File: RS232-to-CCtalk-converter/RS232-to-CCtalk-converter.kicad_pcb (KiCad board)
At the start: 2 copper layers, 23 parts, among them J1 DB9_Male, J2 Conn_01x04, J3 Conn_01x03, Q1 BC847, Q2 BC856A-QR, U1 ST232BDR, U2 UA78M05

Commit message: inital adding
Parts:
- C1, C2, C3, C4, C5, C6, C7, C8, C9: footprint Capacitor_SMD:C_0201_0603Metric -> RS232-to-CCtalk-converter-lib:C_0603_1608Metric
- D1, D2: footprint Diode_SMD:D_SOD-323F -> RS232-to-CCtalk-converter-lib:D_SOD-323F
- J1: footprint Connector_Dsub:DSUB-9_Male_EdgeMount_P2.77mm -> RS232-to-CCtalk-converter-lib:DSUB-9_Male_EdgeMount_P2.77mm
- J2: footprint Connector:FanPinHeader_1x04_P2.54mm_Vertical -> RS232-to-CCtalk-converter-lib:FanPinHeader_1x04_P2.54mm_Vertical
- J3: footprint Connector:FanPinHeader_1x03_P2.54mm_Vertical -> RS232-to-CCtalk-converter-lib:FanPinHeader_1x03_P2.54mm_Vertical
- Q1: footprint Package_TO_SOT_SMD:SOT-23 -> RS232-to-CCtalk-converter-lib:SOT-23
- Q2: value BC856A-QR -> BC856; footprint Package_TO_SOT_SMD:SOT-23 -> RS232-to-CCtalk-converter-lib:SOT-23
- R1, R3, R4: value 10k -> 10K; footprint Resistor_SMD:R_0603_1608Metric -> RS232-to-CCtalk-converter-lib:R_0603_1608Metric
- R2: footprint Resistor_SMD:R_0603_1608Metric -> RS232-to-CCtalk-converter-lib:R_0603_1608Metric
- R5: value 100k -> 100K; footprint Resistor_SMD:R_0603_1608Metric -> RS232-to-CCtalk-converter-lib:R_0603_1608Metric
- U1: value ST232BDR -> ST232B; footprint Package_SO:SOIC-16_4.55x10.3mm_P1.27mm -> RS232-to-CCtalk-converter-lib:SOIC-16_4.55x10.3mm_P1.27mm
- U2: value UA78M05 -> L7805; footprint Package_TO_SOT_SMD:TO-252-3_TabPin2 -> RS232-to-CCtalk-converter-lib:TO-252-3_TabPin2
- moved D1 88.3 mm to (115.5, 100.4)
- moved U2 73.7 mm to (119.4, 94.9)
- moved Q1 46.8 mm to (160.9, 73.5)
- moved C7 44.0 mm to (160.5, 77.0)
- moved C5 41.5 mm to (165.3, 72.6)
- moved J3 30.4 mm to (147.1, 70.4)
- moved J2 28.4 mm to (144.8, 76.2)
- moved R1 28.2 mm to (158.0, 80.6)
- moved R2 24.4 mm to (145.2, 94.6)
- moved C4 16.4 mm to (148.3, 88.5)
- moved R4 14.4 mm to (152.3, 88.5)
- moved R3 14.2 mm to (165.3, 75.1)
- moved R5 9.15 mm to (146.1, 92.1)
- moved C6 7.78 mm to (141.2, 99.1)
- moved C1 7.62 mm to (137.2, 99.1)
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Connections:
- C1 pad 1: Net-(C1-Pad1) -> +5V
- C1 pad 2: +5V -> Net-(C1-Pad2)
- C2 pad 1: GNDREF -> Net-(C2-Pad1)
- C2 pad 2: Net-(C2-Pad2) -> GNDREF
- C3 pad 1: Net-(C3-Pad1) -> Net-(U1-Pad4)
- R1 pad 1: CCTALK-DATA -> +5V
- R1 pad 2: +5V -> CCTALK-DATA
- R4 pad 1: Net-(Q1-Pad1) -> Net-(Q2-Pad3)
- R4 pad 2: Net-(Q2-Pad3) -> Net-(Q1-Pad1)
- R5 pad 1: Net-(Q1-Pad1) -> GNDREF
- R5 pad 2: GNDREF -> Net-(Q1-Pad1)
- U1 pad 1: Net-(C6-Pad2) -> Net-(C6-Pad1)
- U1 pad 2: Net-(C1-Pad1) -> Net-(C1-Pad2)
- U1 pad 3: Net-(C6-Pad1) -> Net-(C6-Pad2)
- U1 pad 4: Net-(C3-Pad2) -> Net-(U1-Pad4)
- U1 pad 5: Net-(C3-Pad1) -> Net-(C3-Pad2)
- U1 pad 6: Net-(C2-Pad2) -> Net-(C2-Pad1)

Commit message: first milestone
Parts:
- C7, C8, C9, D2, U2: moved to B.Cu
- J3: value Conn_01x03 -> CCtalk Cable
- moved C5 62.3 mm to (109.5, 100.2), turned to 180 degrees
- moved R3 55.9 mm to (115.3, 100.0)
- moved Q1 42.9 mm to (123.2, 94.1)
- moved C4 41.0 mm to (109.5, 101.7), turned to 180 degrees
- moved C7 40.8 mm to (122.9, 93.1), turned to -90 degrees
- moved R1 34.7 mm to (126.6, 95.4)
- moved R4 32.5 mm to (120.5, 95.2), turned to 90 degrees
- moved J3 31.1 mm to (129.7, 96.2), turned to 90 degrees
- moved J2 29.2 mm to (117.7, 87.1), turned to 180 degrees
- moved R5 26.0 mm to (120.1, 92.2), turned to -90 degrees
- moved C1 25.1 mm to (112.1, 101.0), turned to 90 degrees
- moved C9 23.7 mm to (119.2, 98.1), turned to 180 degrees
- moved C6 22.8 mm to (118.5, 96.8), turned to 90 degrees
- moved C8 22.5 mm to (118.8, 99.6), turned to 180 degrees
- moved Q2 20.3 mm to (118.6, 100.1), turned to 65 degrees
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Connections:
- J3 pad 1: Net-(D2-Pad2) -> GNDREF
- J3 pad 3: GNDREF -> Net-(D2-Pad2)
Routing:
- net GNDREF: track 0.00 -> 77.8 mm, vias 0 -> 8
- net +5V: track 0.00 -> 29.3 mm, vias 0 -> 1
- net TX: track 0.00 -> 21.5 mm
- net RX: track 0.00 -> 17.4 mm, vias 0 -> 1
- net Net-(C1-Pad2): track 0.00 -> 8.53 mm
- net TXout: track 0.00 -> 8.46 mm, vias 0 -> 2
- net CCTALK-DATA: track 0.00 -> 5.36 mm
- net +24V: track 0.00 -> 4.56 mm
- net RXout: track 0.00 -> 4.55 mm
- net Net-(Q1-Pad1): track 0.00 -> 3.77 mm
- net Net-(Q2-Pad3): track 0.00 -> 3.62 mm
- net Net-(D2-Pad2): track 0.00 -> 3.14 mm
- net Net-(C6-Pad1): track 0.00 -> 2.18 mm
- net Net-(C2-Pad1): track 0.00 -> 2.00 mm
- net Net-(C3-Pad2): track 0.00 -> 1.93 mm
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- added copper zone on B.Cu, net GNDREF
- added copper zone on F.Cu, net GNDREF
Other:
- board outline added: 30.4 x 16.9 mm
- board text added: "+24 CC GND"

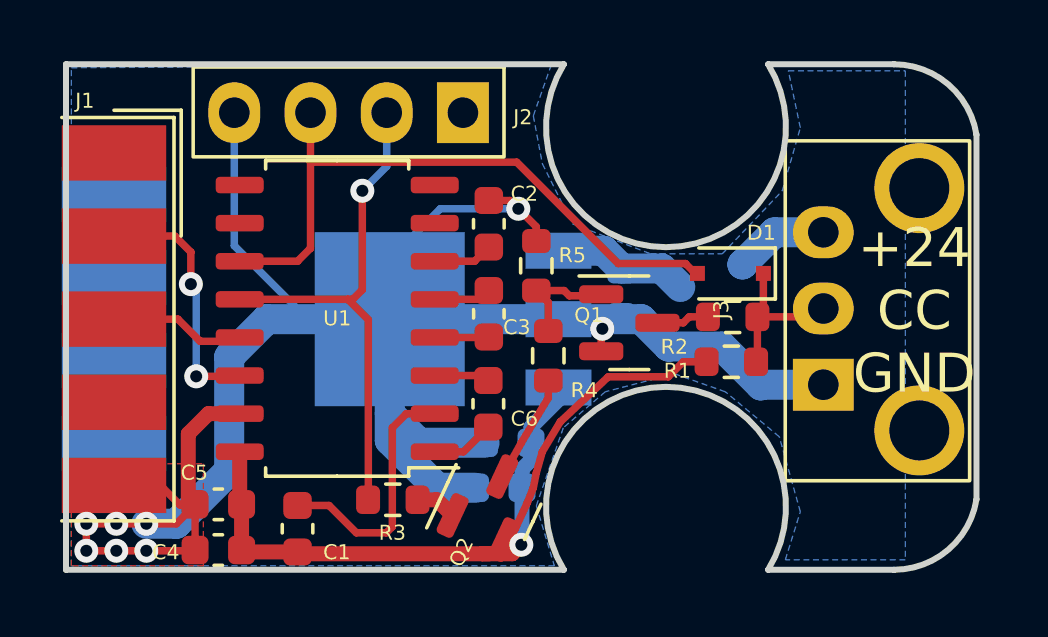
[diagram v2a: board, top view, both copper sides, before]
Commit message: add +5v to debug connector
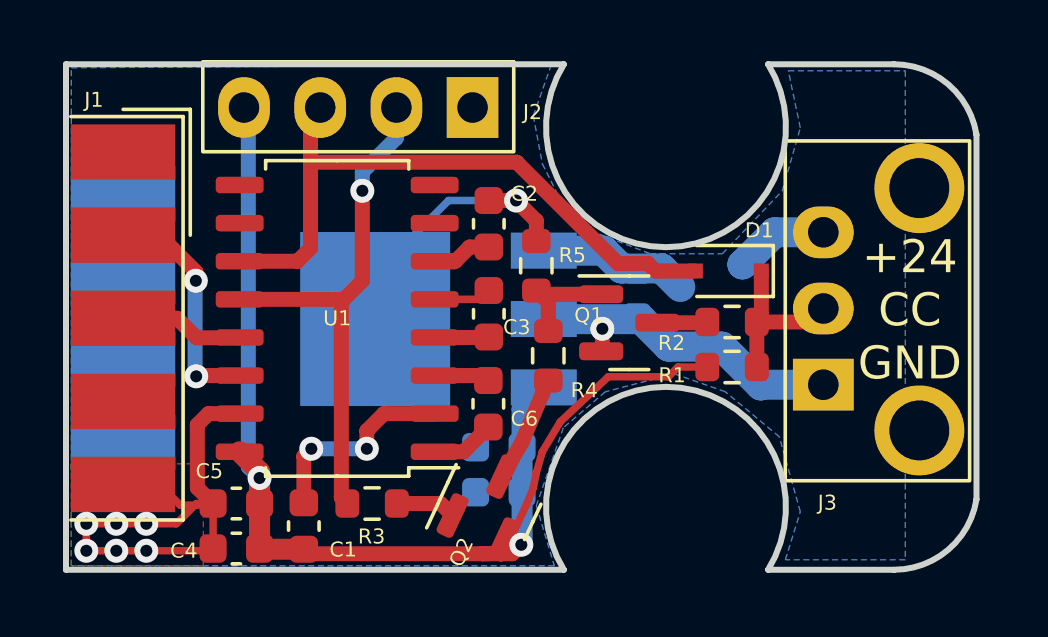
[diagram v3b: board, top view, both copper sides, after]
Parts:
- moved R3 0.70 mm to (114.6, 100.1)
- moved C4 0.60 mm to (110.1, 101.6)
- moved C5 0.60 mm to (110.1, 100.1)
- moved C7 0.51 mm to (123.5, 93.1)
- moved U2 0.49 mm to (116.2, 94.0)
- moved J2 0.37 mm to (118.0, 86.9)
- moved C9 0.34 mm to (118.8, 98.2)
- moved J1 0.30 mm to (106.3, 94.0)
- moved C1 0.23 mm to (112.3, 100.9)
- moved R1 0.18 mm to (126.6, 95.6)
- moved R2 0.17 mm to (126.6, 94.1)
- moved C8 0.15 mm to (118.8, 99.8)
- moved D1 0.11 mm to (126.5, 92.4)
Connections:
- J2 pad 1: +5V -> GNDREF
- J2 pad 4: GNDREF -> +5V
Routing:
- net GNDREF: track 77.8 -> 39.6 mm
- net +5V: track 29.3 -> 40.8 mm, vias 1 -> 2
- net TX: track 21.5 -> 25.9 mm
- net Net-(C1-Pad2): track 8.53 -> 6.67 mm, vias 0 -> 2
- net Net-(Q2-Pad1): track 1.39 -> 2.03 mm
- net TXout: track 8.46 -> 7.90 mm

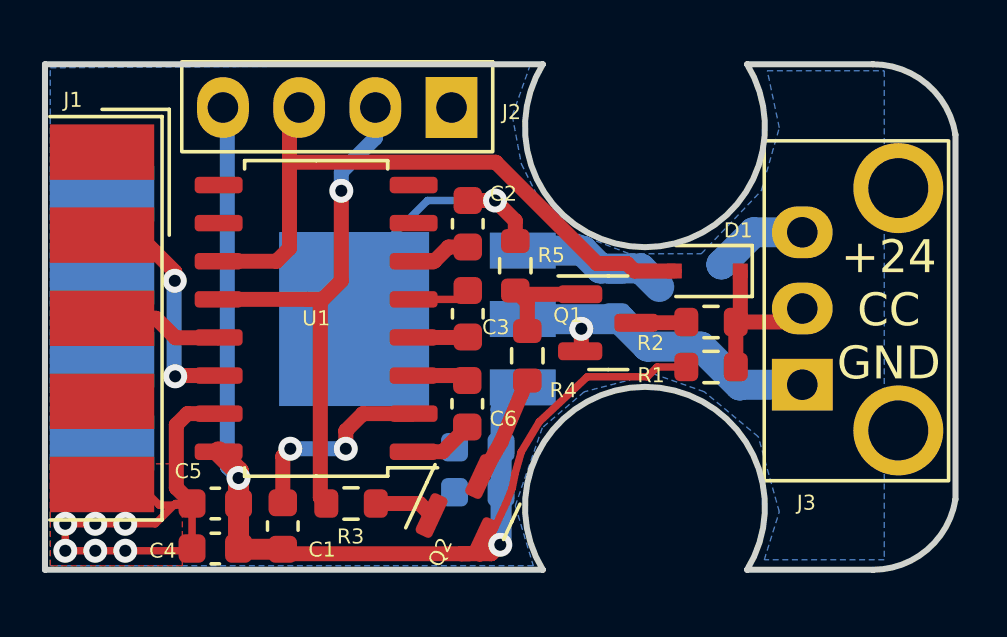
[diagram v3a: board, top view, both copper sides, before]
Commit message: remove +5V on debug connector
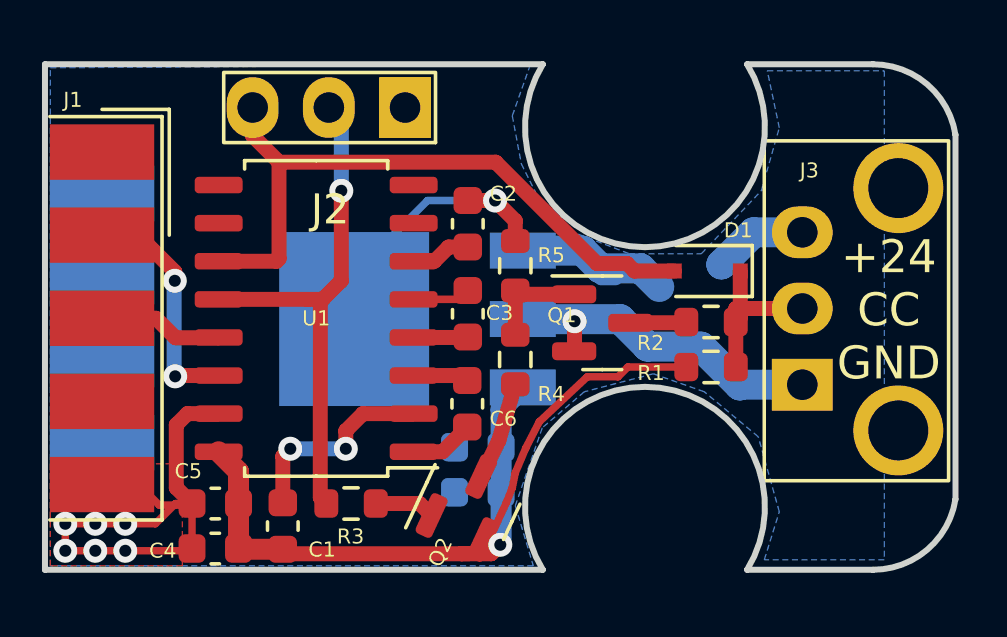
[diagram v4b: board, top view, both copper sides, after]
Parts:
- J2: value Conn_01x04 -> CCtalk Cable; footprint RS232-to-CCtalk-converter-lib:FanPinHeader_1x04_P2.54mm_Vertical -> RS232-to-CCtalk-converter-lib:Header_1x03_P2.54mm_Vertical
- J3: footprint RS232-to-CCtalk-converter-lib:FanPinHeader_1x03_P2.54mm_Vertical -> RS232-to-CCtalk-converter-lib:Header_1x03_P2.54mm_Vertical_with_holder
- moved J2 1.55 mm to (116.4, 86.9)
- moved R4 0.42 mm to (120.1, 95.3)
- moved C7 0.25 mm to (123.2, 93.2)
- moved Q1 0.20 mm to (123.0, 94.1)
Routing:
- net +5V: track 40.8 -> 28.3 mm, vias 2 -> 1
- net TX: track 25.9 -> 22.1 mm

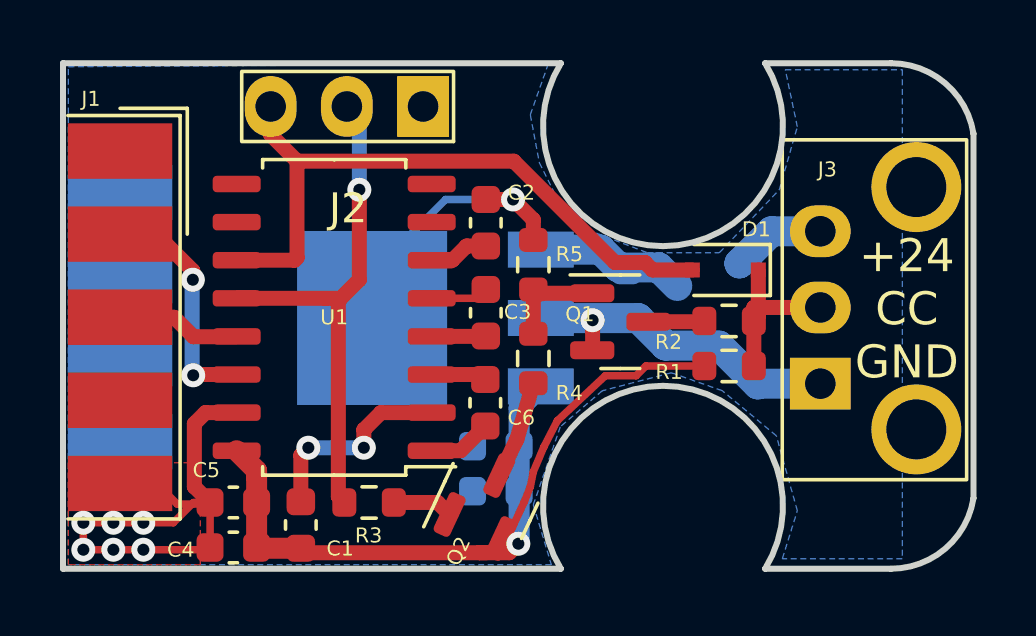
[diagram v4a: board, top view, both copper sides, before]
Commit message: add labels for the debug conn
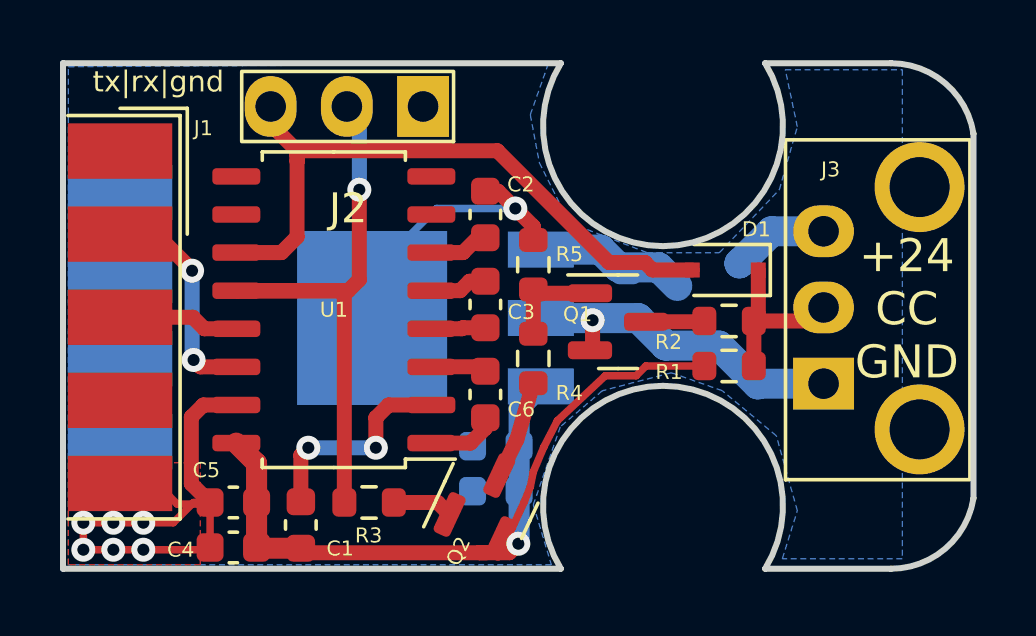
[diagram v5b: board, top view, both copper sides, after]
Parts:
- moved C2 0.28 mm to (118.5, 90.5)
- moved C3 0.28 mm to (118.5, 93.5)
- moved C6 0.27 mm to (118.5, 96.5)
- moved U1 0.25 mm to (113.5, 93.7)
- moved J3 0.11 mm to (129.8, 96.2)
- moved Q1 0.08 mm to (122.9, 94.1)
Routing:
- net RX: track 17.2 -> 20.9 mm
- net Net-(C1-Pad2): track 6.67 -> 7.18 mm
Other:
- board text added: "tx|rx|gnd"

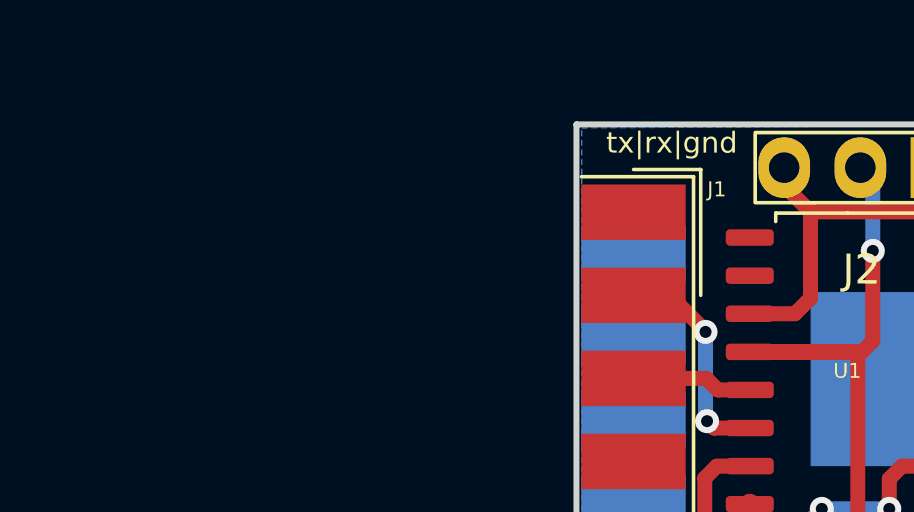
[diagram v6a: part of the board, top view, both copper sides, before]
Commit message: replace 3d model db9; add new mpn db9; generate new outputs
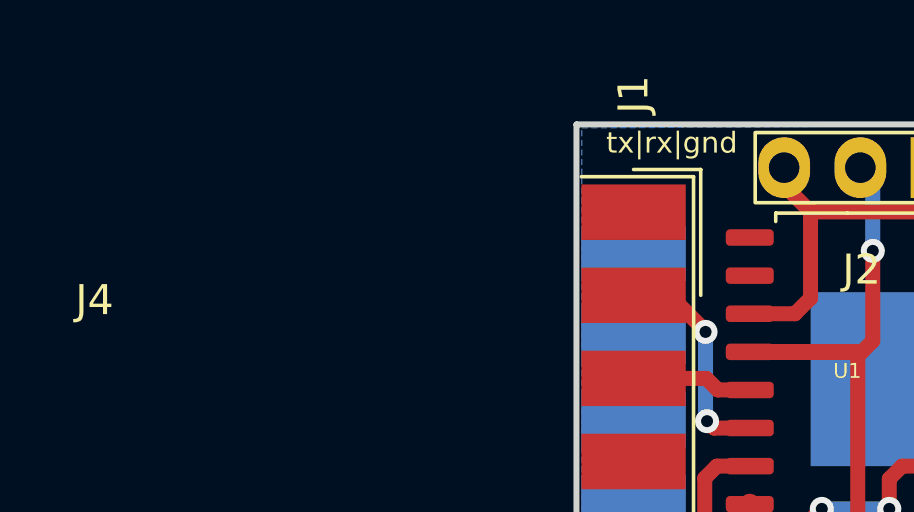
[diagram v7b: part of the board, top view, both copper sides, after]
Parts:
- added J4: DB9_female_hood, RS232-to-CCtalk-converter-lib:DSUB-9_Female_wire_mount_P2.77mm_hood, F.Cu at (119.5, 94.0)
- J1: value DB9_Male -> DB9_Female
